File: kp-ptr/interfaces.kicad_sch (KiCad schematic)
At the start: 12 parts, among them IC1 E22-900M22S, J4 USB_C_Receptacle_USB2.0, J5 Micro_SD_Card_Det, U10 USBLC6-2SC6

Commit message: Small changes before sleep Signed-off-by: kretu <krecik@gmail.com>
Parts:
- J5: footprint (none) -> KP-PTR_lib:GCT_MEM2051-00-195-00-A
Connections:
- net Earth: no longer J5.11 (SHIELD)
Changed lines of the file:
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@@
   (symbol (lib_id "Connector:Micro_SD_Card_Det") (at 137.16 105.41 0) (unit 1)
     (in_bom yes) (on_board yes) (fields_autoplaced)
-    (property "Reference" "J5" (id 0) (at 137.795 83.82 0))
-    (property "Value" "Micro_SD_Card_Det" (id 1) (at 137.795 86.36 0))
-    (property "Footprint" "" (id 2) (at 189.23 87.63 0)
+    (property "Reference" "J5" (id 0) (at 158.75 104.1399 0)
+      (effects (font (size 1.27 1.27)) (justify left))
+    )
+    (property "Value" "Micro_SD_Card_Det" (id 1) (at 158.75 106.6799 0)
+      (effects (font (size 1.27 1.27)) (justify left))
+    )
+    (property "Footprint" "KP-PTR_lib:GCT_MEM2051-00-195-00-A" (id 2) (at 189.23 87.63 0)
       (effects (font (size 1.27 1.27)) hide)
     )
@@
     )
     (pin "1")
-    (pin "10")
-    (pin "11")
     (pin "2")
     (pin "3")

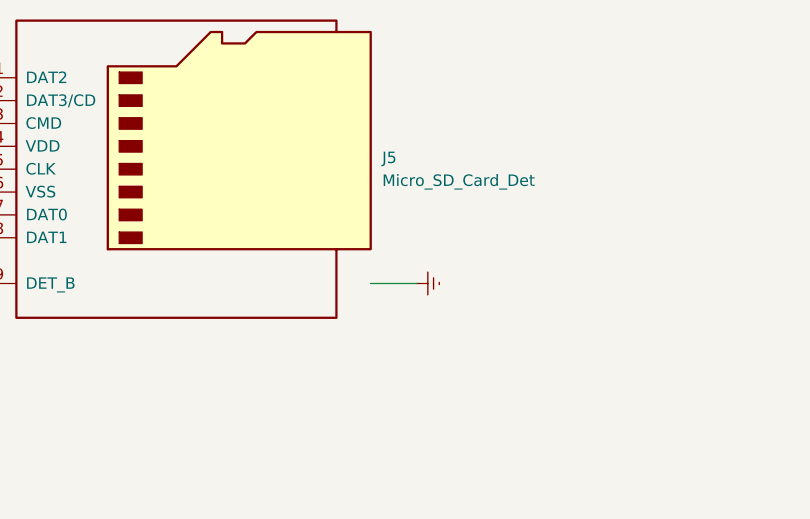
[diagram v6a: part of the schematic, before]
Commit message: Golaiath fight with board Signed-off-by: kretu <krecik@gmail.com>
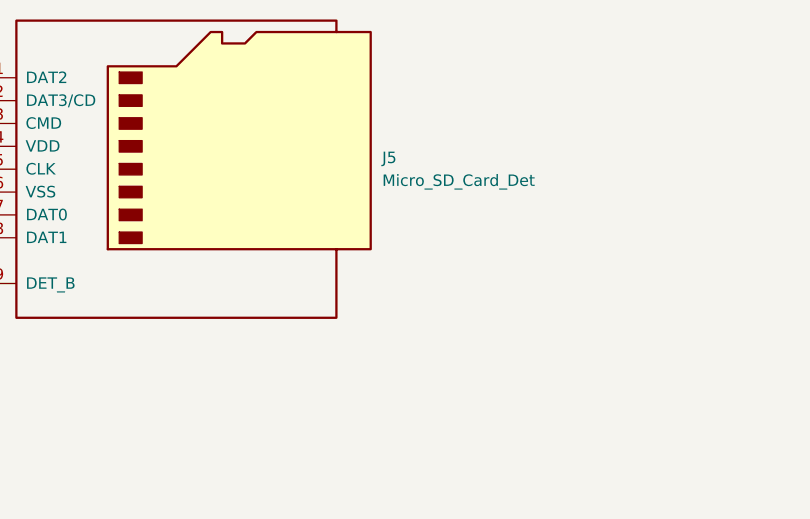
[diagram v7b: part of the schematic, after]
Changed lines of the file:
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@@
-    (stroke (width 0) (type default) (color 0 0 0 0))
-  )
-  (wire (pts (xy 162.56 118.11) (xy 157.48 118.11))
     (stroke (width 0) (type default) (color 0 0 0 0))
   )
@@
     (pin "9")
   )
-  (symbol (lib_id "power:Earth") (at 162.56 118.11 90) (unit 1)
-    (in_bom yes) (on_board yes) (fields_autoplaced)
-    (property "Reference" "#PWR0122" (id 0) (at 168.91 118.11 0)
-      (effects (font (size 1.27 1.27)) hide)
-    )
-    (property "Value" "Earth" (id 1) (at 166.37 118.11 0)
-      (effects (font (size 1.27 1.27)) hide)
-    )
-    (property "Footprint" "" (id 2) (at 162.56 118.11 0)
-      (effects (font (size 1.27 1.27)) hide)
-    )
-    (property "Datasheet" "~" (id 3) (at 162.56 118.11 0)
-      (effects (font (size 1.27 1.27)) hide)
-    )
-    (pin "1")
-  )
   (symbol (lib_id "power:Earth") (at 234.95 85.09 0) (unit 1)

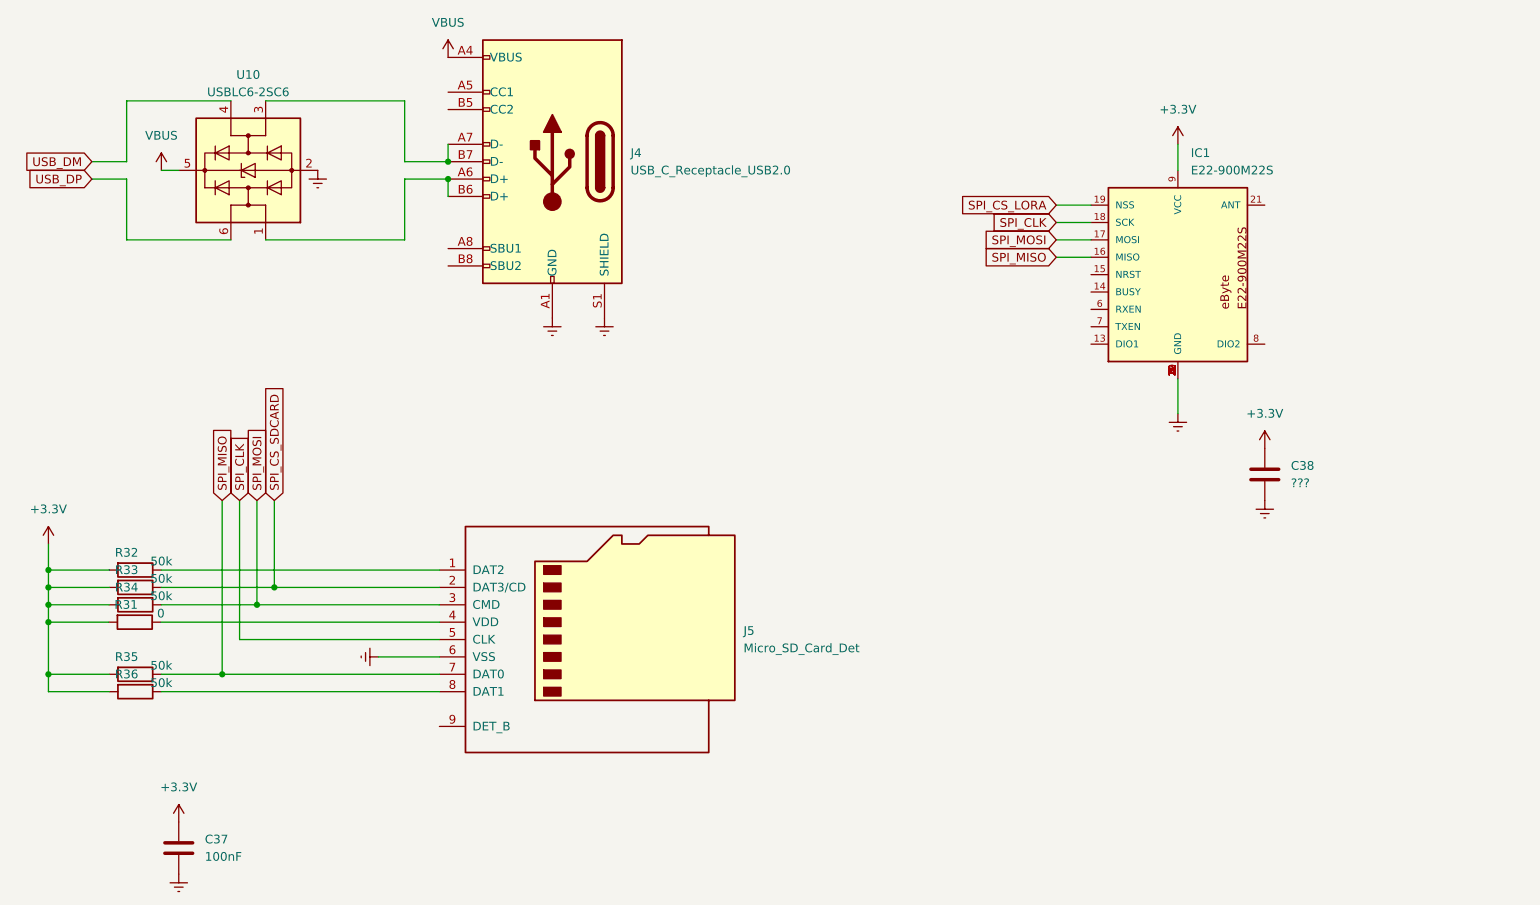
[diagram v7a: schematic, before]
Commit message: RF added, multiple small changes
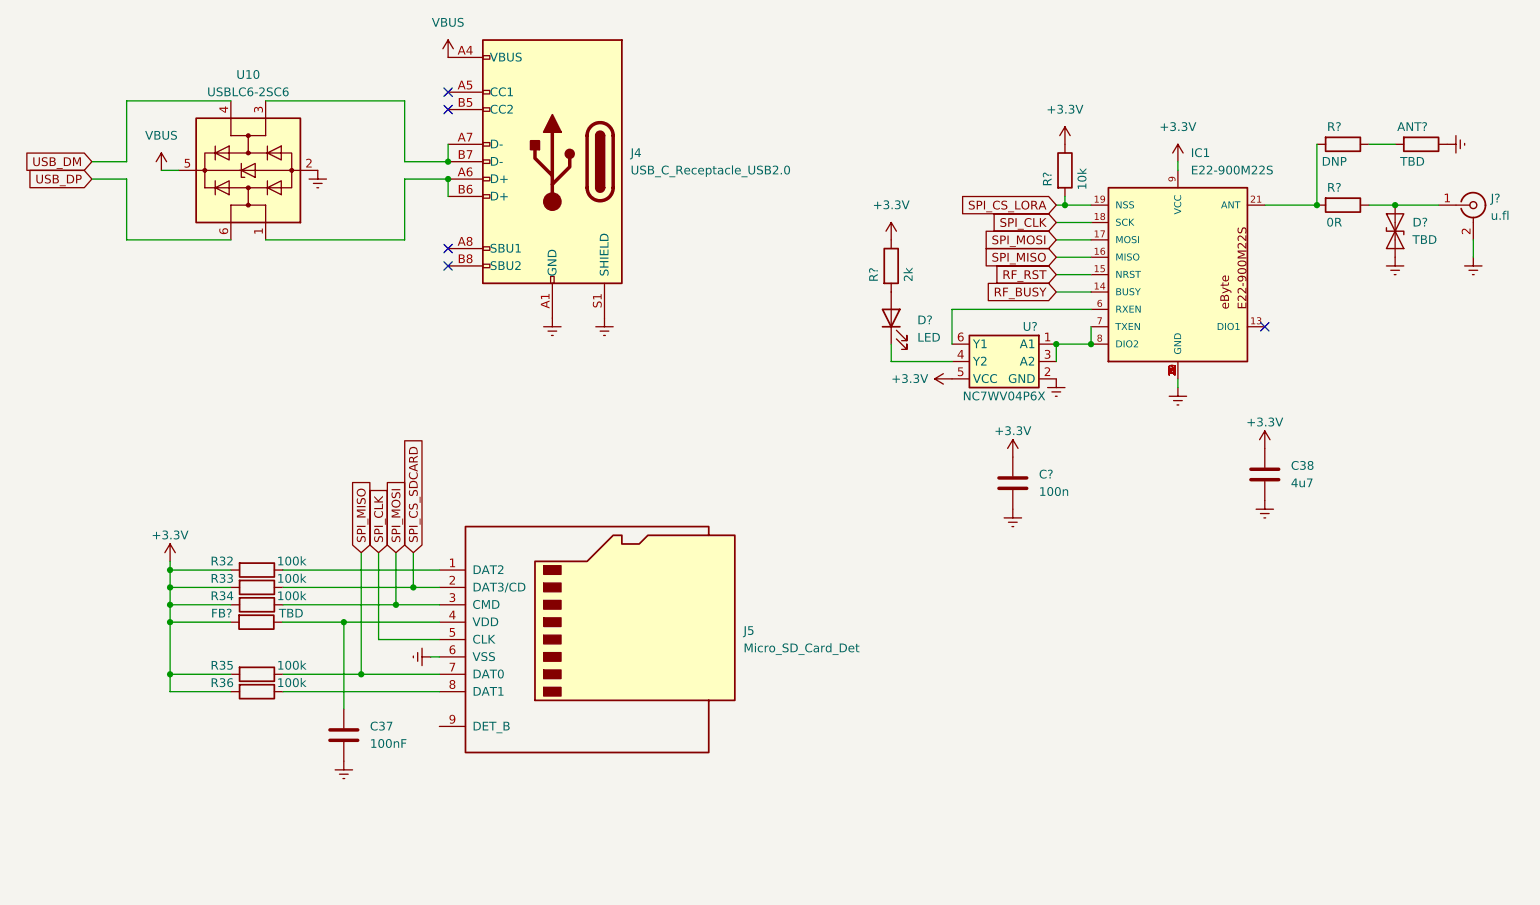
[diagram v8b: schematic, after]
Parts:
- added ANT?: TBD, Resistor_SMD:R_0402_1005Metric_Pad0.72x0.64mm_HandSolder, symbol Device:R
- added C?: 100n, Capacitor_SMD:C_0402_1005Metric_Pad0.74x0.62mm_HandSolder, symbol Device:C
- added D?: TBD, symbol Diode:ESD9B3.3ST5G
- added D?: LED, LED_SMD:LED_0402_1005Metric_Pad0.77x0.64mm_HandSolder, symbol Device:LED
- added J?: u.fl, symbol Connector:Conn_Coaxial
- added R?: DNP, Resistor_SMD:R_0402_1005Metric_Pad0.72x0.64mm_HandSolder, symbol Device:R
- added R?: 10k, Resistor_SMD:R_0402_1005Metric_Pad0.72x0.64mm_HandSolder, symbol Device:R
- added R?: 0R, Resistor_SMD:R_0402_1005Metric_Pad0.72x0.64mm_HandSolder, symbol Device:R
- added R?: 2k, Resistor_SMD:R_0402_1005Metric_Pad0.72x0.64mm_HandSolder, symbol Device:R
- added U?: NC7WV04P6X, symbol KP-PTR_lib:NC7WV04P6X
- C38: value ??? -> 4u7; footprint Capacitor_SMD:C_01005_0402Metric_Pad0.57x0.30mm_HandSolder -> Capacitor_SMD:C_0805_2012Metric_Pad1.18x1.45mm_HandSolder
- FB?: renamed from R31; value 0 -> TBD
- R32, R33, R34, R35, R36: value 50k -> 100k
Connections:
- net +3V3: now also C?.1, R?.1, R?.1, U?.5 (VCC); no longer C37.1
- net Earth: now also ANT?.1, C?.2, D?.1 (A1), J?.2 (Ext), U?.2 (GND)
- net SPI_CS_LORA: now also R?.2
- net at FB?.1, J5.4 (VDD): now also C37.1
- net RF_BUSY: now reaches IC1.14 (BUSY)
- net RF_RST: now reaches IC1.15 (NRST)
- net at IC1.21 (ANT): now also R?.2, R?.2
- net at IC1.6 (RXEN): now also U?.6 (Y1)
- net at IC1.7 (TXEN): now also IC1.8 (DIO2), U?.1 (A1), U?.3 (A2)
- new net: D?.1 (K), U?.4 (Y2)
- new net: D?.2 (A2), J?.1 (In), R?.1
- new net: ANT?.2, R?.1
- new net: D?.2 (A), R?.2
- no-connect marks 0 -> 5
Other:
- moved on the sheet: C37, FB?, R32, R33, R34, R35, R36
